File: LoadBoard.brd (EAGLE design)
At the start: 99 x 99 mm, 105 parts, among them IC1 7805TV, IC2 LM358D, IC3 MCP23S17SO, IC4 ATMEGA328P_TQFP, IC5 MAX232SOIC16, IC6 MCP4921, IC7 TL431CD, IC8 DS18B20, IC9 DS18B20, Q1 IRF3710, Q2 16MHz, Q3 IRF3710, T1 BC817, T2 BC817, U4 IRLML2502, U9 IRLML2502

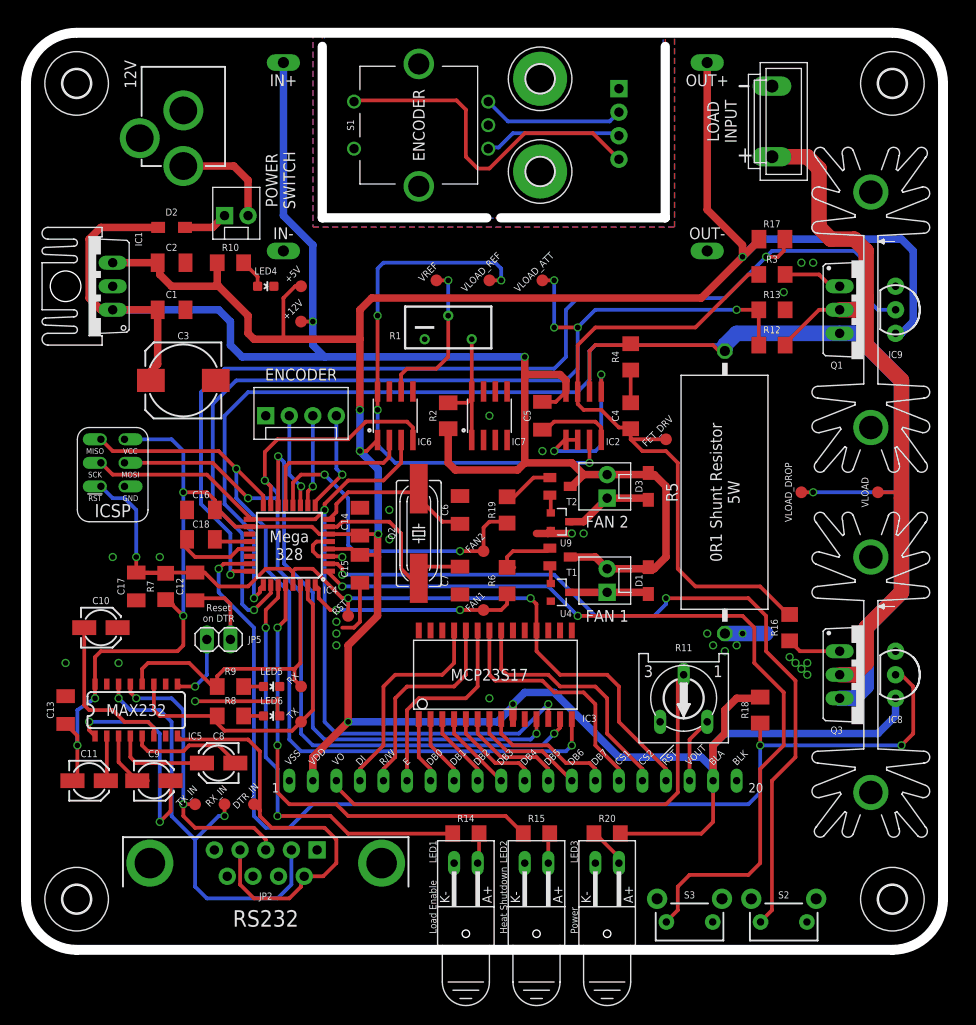
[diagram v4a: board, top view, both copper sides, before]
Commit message: added fiducials to the board
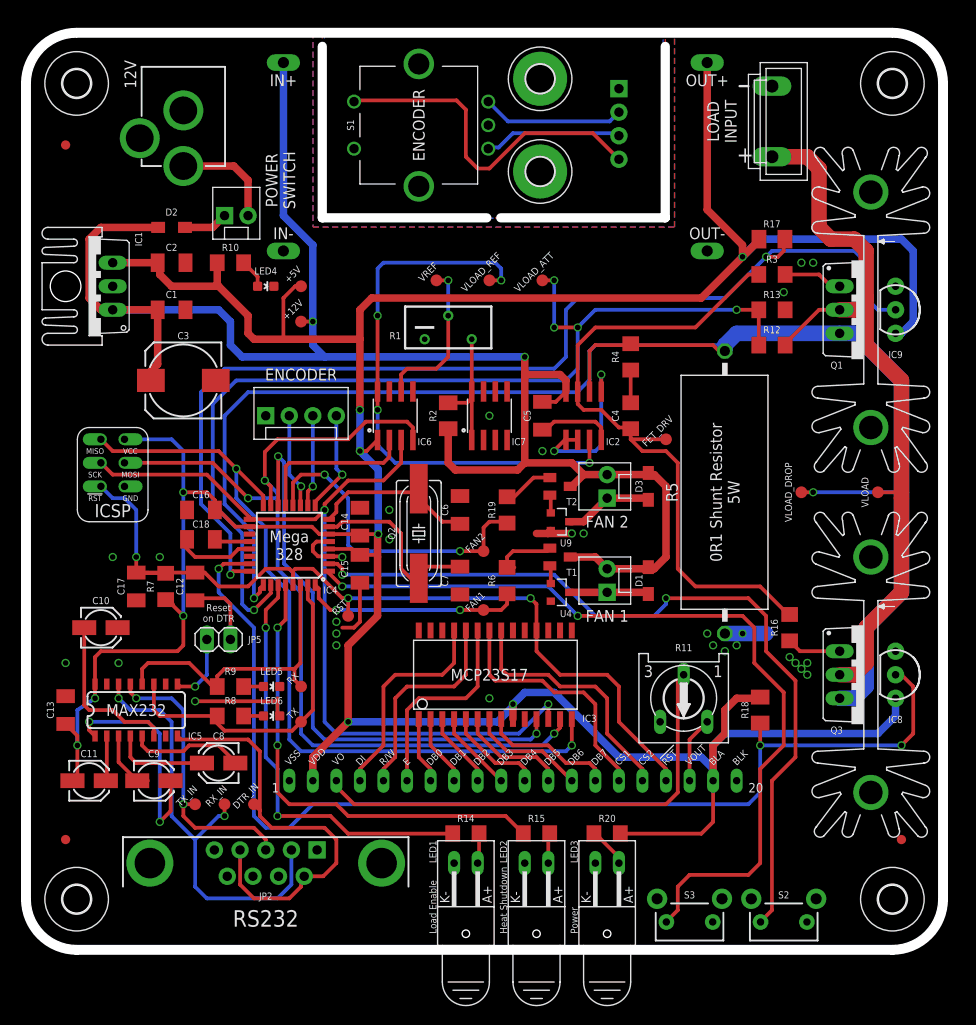
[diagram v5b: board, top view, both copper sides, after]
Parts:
- added FID1, FID2, FID3: FIDUCIAL1X2, SparkFun-Aesthetics:FIDUCIAL-1X2
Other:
- board text added: "github.com/dangrie158/SmartDummyLoad"
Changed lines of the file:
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@@
 <grid distance="0.05" unitdist="inch" unit="mil" style="dots" multiple="1" display="yes" altdistance="0.025" altunitdist="inch" altunit="inch"/>
 <layers>
-<layer number="1" name="Top" color="4" fill="1" visible="no" active="yes"/>
+<layer number="1" name="Top" color="4" fill="1" visible="yes" active="yes"/>
 <layer number="2" name="Route2" color="1" fill="3" visible="no" active="no"/>
 <layer number="3" name="Route3" color="4" fill="3" visible="no" active="no"/>
@@
 <layer number="19" name="Unrouted" color="6" fill="1" visible="yes" active="yes"/>
 <layer number="20" name="Dimension" color="15" fill="1" visible="yes" active="yes"/>
-<layer number="21" name="tPlace" color="7" fill="1" visible="no" active="yes"/>
+<layer number="21" name="tPlace" color="7" fill="1" visible="yes" active="yes"/>
 <layer number="22" name="bPlace" color="7" fill="1" visible="yes" active="yes"/>
-<layer number="23" name="tOrigins" color="15" fill="1" visible="no" active="yes"/>
+<layer number="23" name="tOrigins" color="15" fill="1" visible="yes" active="yes"/>
 <layer number="24" name="bOrigins" color="15" fill="1" visible="yes" active="yes"/>
-<layer number="25" name="tNames" color="7" fill="1" visible="no" active="yes"/>
+<layer number="25" name="tNames" color="7" fill="1" visible="yes" active="yes"/>
 <layer number="26" name="bNames" color="7" fill="1" visible="yes" active="yes"/>
-<layer number="27" name="tValues" color="7" fill="1" visible="no" active="yes"/>
+<layer number="27" name="tValues" color="7" fill="1" visible="yes" active="yes"/>
 <layer number="28" name="bValues" color="7" fill="1" visible="yes" active="yes"/>
 <layer number="29" name="tStop" color="7" fill="3" visible="no" active="yes"/>
@@
 </polygon>
 <text x="16.51" y="93.98" size="1.27" layer="26" rot="MR0" align="bottom-center">12V IN</text>
+<text x="74.93" y="35.56" size="1.27" layer="26" rot="MR0" align="bottom-center">github.com/dangrie158/SmartDummyLoad</text>
 </plain>
 <attributes>
@@
 <element name="U$1" library="OwnStuff" package="LOGO-SILKSCREEN" value="" x="80.01" y="51.435" rot="MR0"/>
 <element name="U$2" library="SparkFun-Aesthetics" package="OSHW-LOGO-L" value="" x="68.58" y="52.07" rot="MR0"/>
+<element name="FID1" library="SparkFun-Aesthetics" package="FIDUCIAL-1X2" value="FIDUCIAL1X2" x="3.81" y="11.43"/>
+<element name="FID2" library="SparkFun-Aesthetics" package="FIDUCIAL-1X2" value="FIDUCIAL1X2" x="3.81" y="86.36"/>
+<element name="FID3" library="SparkFun-Aesthetics" package="FIDUCIAL-1X2" value="FIDUCIAL1X2" x="93.98" y="11.43"/>
 </elements>
 <signals>

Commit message: added documentation to bottom of board
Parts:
- moved U$1 33.5 mm to (46.5, 50.4)
- moved U$2 12.0 mm to (56.6, 51.1)
